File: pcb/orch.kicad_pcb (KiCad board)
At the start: 2 copper layers, 313.6 x 80.8 mm, 139 parts, among them J1 AVR-ISP-6, P1 USB_C_Receptacle_USB2.0, SW1 MX-NoLED, SW10 MX-NoLED, SW11 MX-NoLED, SW12 MX-NoLED, SW13 MX-NoLED, SW14 MX-NoLED, SW15 MX-NoLED, SW16 MX-NoLED, SW17 MX-NoLED, SW18 MX-NoLED, SW19 MX-NoLED, SW2 MX-NoLED, SW20 MX-NoLED, SW21 MX-NoLED, SW22 MX-NoLED, SW23 MX-NoLED, SW24 MX-NoLED, SW25 MX-NoLED, SW26 MX-NoLED, SW27 MX-NoLED, SW28 MX-NoLED, SW29 MX-NoLED, SW3 MX-NoLED, SW30 MX-NoLED, SW31 MX-NoLED, SW32 MX-NoLED, SW33 MX-NoLED, SW34 MX-NoLED, SW35 MX-NoLED, SW36 MX-NoLED, SW37 MX-NoLED, SW38 MX-NoLED, SW39 MX-NoLED, SW4 MX-NoLED, SW40 MX-NoLED, SW41 MX-NoLED, SW42 MX-NoLED, SW43 MX-NoLED, SW44 MX-NoLED, SW45 MX-NoLED, SW46 MX-NoLED, SW47 MX-NoLED, SW48 MX-NoLED, SW49 MX-NoLED, SW5 MX-NoLED, SW50 MX-NoLED, SW51 MX-NoLED, SW52 MX-NoLED, SW53 MX-NoLED, SW54 MX-NoLED, SW55 MX-NoLED, SW56 MX-NoLED, SW57 MX-NoLED, SW58 Reset, SW6 MX-NoLED, SW7 MX-NoLED, SW8 MX-NoLED, SW9 MX-NoLED, U1 ATmega32U4-AU, Y1 16MHz

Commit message: logo
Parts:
- added G***: LOGO, orch:model, B.Cu at (115.6, 177.3)
- added G***: LOGO, orch:logo_small, B.Cu at (240.3, 177.5)
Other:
- board text removed: "orch v0.0.1"

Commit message: new logos
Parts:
- removed the G*** at (115.6, 177.3)
- removed the G*** at (240.3, 177.5)
- added G***: LOGO, orch:htpkbs, B.Cu at (239.8, 177.3)
- added G***: LOGO, orch:orch, B.Cu at (118.4, 177.3)

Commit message: move logos
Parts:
- moved G*** 2.45 mm to (237.4, 176.6)
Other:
- board text added: "htpkbs.com 2021"

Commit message: fix rows and start new traces
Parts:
- moved C4 55.6 mm to (346.4, 154.8), turned to 45 degrees
- moved C3 50.1 mm to (344.0, 144.0), turned to 315 degrees
- moved C5 48.5 mm to (333.2, 159.8), turned to 135 degrees
- moved C6 32.9 mm to (328.2, 146.8), turned to 225 degrees
- moved R5 32.4 mm to (345.2, 117.6)
- moved R4 30.3 mm to (345.2, 114.0)
- moved C7 29.5 mm to (333.0, 141.7), turned to 45 degrees
- moved C8 23.8 mm to (343.4, 130.8), turned to 90 degrees
- moved F1 10.2 mm to (339.3, 115.8), turned to 90 degrees
- moved R6 5.29 mm to (327.9, 154.4), turned to 315 degrees
- moved R2 4.33 mm to (336.3, 130.8)
- moved R1 3.81 mm to (362.7, 138.2)
- moved SW58 3.66 mm to (357.1, 138.2)
- moved J1 3.30 mm to (349.8, 138.2)
- moved R3 2.68 mm to (339.9, 130.8)
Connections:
- U1 pad 36: Net-(U1-Pad36) -> /Row4
- U1 pad 37: Net-(U1-Pad37) -> /Row3
- U1 pad 38: Net-(U1-Pad38) -> /Row2
- U1 pad 39: Net-(U1-Pad39) -> /Row1
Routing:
- net /Col3: track 364.6 -> 0.00 mm, vias 1 -> 0
- net +5V: track 411.1 -> 65.6 mm, vias 12 -> 0
- net /Col1: track 321.2 -> 0.00 mm, vias 1 -> 0
- net /Col5: track 320.2 -> 0.00 mm, vias 1 -> 0
- net /Col2: track 315.5 -> 0.00 mm, vias 1 -> 0
- net /Col6: track 295.5 -> 0.00 mm, vias 1 -> 0
- net /Row3: track 291.3 -> 0.00 mm
- net /Row2: track 287.4 -> 0.00 mm
- net /Row4: track 287.3 -> 0.00 mm
- net /Row1: track 286.7 -> 0.00 mm
- net /Col4: track 279.2 -> 0.00 mm, vias 1 -> 0
- net /Col8: track 239.8 -> 0.00 mm, vias 1 -> 0
- net /Col7: track 196.8 -> 0.00 mm, vias 1 -> 0
- net /Col9: track 170.4 -> 0.00 mm, vias 1 -> 0
- net /Col11: track 157.7 -> 0.00 mm
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
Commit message: v1.0.0
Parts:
- removed the G*** at (118.4, 177.3)
- moved G*** 130.6 mm to (120.1, 119.1)
- turned SW58 to 180 degrees
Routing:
- net +5V: track 65.6 -> 391.6 mm, vias 0 -> 5
- net /Row1: track 0.00 -> 324.0 mm, vias 0 -> 1
- net /Col1: track 0.00 -> 320.8 mm
- net /Row4: track 0.00 -> 320.7 mm, vias 0 -> 3
- net /Row2: track 0.00 -> 308.3 mm, vias 0 -> 1
- net /Col2: track 0.00 -> 302.4 mm
- net /Row3: track 0.00 -> 300.2 mm, vias 0 -> 1
- net /Col3: track 0.00 -> 284.2 mm
- net /Col4: track 0.00 -> 261.7 mm
- net /Col5: track 0.00 -> 238.7 mm
- net /Col6: track 0.00 -> 215.2 mm
- net /Col7: track 0.00 -> 190.0 mm, vias 0 -> 1
- net /Col8: track 0.00 -> 182.8 mm
- net /Col9: track 0.00 -> 165.5 mm
- net /Col10: track 0.00 -> 148.6 mm
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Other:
- board text added: "hack the planet"
- board text added: "orch v1.0.0 2021"
- board text removed: "htpkbs.com 2021"

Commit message: redo power
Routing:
- net +5V: track 391.6 -> 402.4 mm, vias 5 -> 6
- net /Col15: track 89.5 -> 91.9 mm
- net /MOSI: track 18.2 -> 20.3 mm
- net /D+: track 15.5 -> 16.8 mm
- net /Reset: track 38.4 -> 39.7 mm
- net /D-: track 14.9 -> 15.7 mm
- net /Col14: track 93.7 -> 93.2 mm, vias 3 -> 4
- net GND: vias 3 -> 7

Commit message: v2!
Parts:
- added D25: 1N4148, orch:D_DO-35_SOD27_P5.08mm_Horizontal, B.Cu at (165.7, 172.6)
- added D29: 1N4148, orch:D_DO-35_SOD27_P5.08mm_Horizontal, B.Cu at (201.1, 172.6)
- added D55: 1N4148, orch:D_DO-35_SOD27_P5.08mm_Horizontal, B.Cu at (348.1, 155.8)
- added D66: SK6812, LED_SMD:LED_SK6812_PLCC4_5.0x5.0mm_P3.2mm, B.Cu at (306.9, 163.8)
- added SW25: MX-NoLED, orch:MX-2U-NoLED, F.Cu at (183.4, 168.6)
- added SW29: MX-NoLED, orch:MX-1U-NoLED, F.Cu at (192.9, 168.6)
- added SW55: Rotary_Encoder_Switch, orch:RotaryEncoder_Alps_EC11E-Switch_Vertical_H20mm, F.Cu at (330.5, 149.4)
- SW24: footprint orch:MX-2U-NoLED -> orch:MX-1U-NoLED
- SW51: renamed from SW49; footprint orch:MX-2.25U-NoLED -> orch:MX-1.75U-NoLED
- moved D63 102.0 mm to (107.4, 121.1)
- moved D65 99.5 mm to (202.4, 159.2)
- moved D62 77.4 mm to (202.4, 121.1)
- moved G*** 71.9 mm to (77.4, 176.9)
- moved D64 45.0 mm to (107.4, 159.1)
- moved R1 26.3 mm to (349.4, 115.5), turned to 90 degrees
- moved D61 23.4 mm to (306.9, 121.2)
- moved C1 23.1 mm to (350.9, 138.7), turned to 45 degrees
- moved C2 23.1 mm to (347.4, 142.2)
- moved Y1 23.1 mm to (345.7, 137.0)
- moved R6 23.0 mm to (326.3, 131.5)
- moved C4 22.6 mm to (345.2, 132.2)
- moved C6 22.4 mm to (327.3, 124.5)
- moved U1 22.4 mm to (336.5, 128.3)
- moved C7 22.1 mm to (332.0, 119.6)
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- renumbered D25 to D26, D26 to D27, D27 to D28, D28 to D30, D29 to D31, D30 to D32, D31 to D33, D32 to D34, D33 to D35, D34 to D36, D35 to D37, D36 to D38, D37 to D39, D38 to D40, D39 to D41, D40 to D42, D41 to D43, D42 to D44, D43 to D45, D44 to D46, D45 to D47, D46 to D48, D47 to D49, D48 to D50, D49 to D51, D50 to D52, D51 to D53, D52 to D54, D53 to D56, D54 to D57, D55 to D58, D56 to D59, D57 to D60, D58 to D61, D59 to D62, D60 to D63, D61 to D64, D62 to D65, SW25 to SW26, SW26 to SW27, SW27 to SW28, SW28 to SW30, SW29 to SW31, SW30 to SW32, SW31 to SW33, SW32 to SW34, SW33 to SW35, SW34 to SW36, SW35 to SW37, SW36 to SW38, SW37 to SW39, SW38 to SW40, SW39 to SW41, SW40 to SW42, SW41 to SW43, SW42 to SW44, SW43 to SW45, SW44 to SW46, SW45 to SW47, SW46 to SW48, SW47 to SW49, SW48 to SW50, SW50 to SW52, SW51 to SW53, SW52 to SW54, SW53 to SW56, SW54 to SW57, SW55 to SW58, SW56 to SW59, SW57 to SW60, SW58 to SW61
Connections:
- U1 pad 1: Net-(U1-Pad1) -> /Col14
- U1 pad 12: /Col14 -> /Row2
- U1 pad 18: /Col13 -> /Row3
- U1 pad 19: /Col12 -> /Row4
- U1 pad 20: /Col11 -> /Col13
- U1 pad 21: /Col10 -> /Col12
- U1 pad 22: /Col9 -> /Col11
- U1 pad 25: /Col8 -> /Col10
- U1 pad 26: /Col7 -> /Col9
- U1 pad 27: /Col6 -> /Col8
- U1 pad 28: /Col5 -> /Col7
- U1 pad 29: /Col4 -> /Col6
- U1 pad 30: /Col3 -> /Col5
- U1 pad 31: /Col2 -> /Col4
- U1 pad 32: /Col1 -> /Col3
- U1 pad 36: /Row4 -> /Col1
- U1 pad 37: /Row3 -> /Col2
- U1 pad 38: /Row2 -> /RGB
- U1 pad 39: /Row1 -> /RotaryA
- U1 pad 40: /RGB -> /RotaryB
- U1 pad 41: /Col15 -> /Row1
- U1 pad 8: Net-(U1-Pad8) -> /Col15
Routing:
- net +5V: track 402.4 -> 590.0 mm, vias 6 -> 9
- net Net-(D65-Pad4): track 0.00 -> 112.8 mm
- net Net-(D64-Pad4): track 39.8 -> 102.3 mm
- net Net-(D61-Pad4): track 41.2 -> 100.9 mm
- net /Row4: track 320.7 -> 361.4 mm, vias 3 -> 0
- net /Row3: track 300.6 -> 337.3 mm, vias 1 -> 2
- net /RotaryB: track 0.00 -> 36.3 mm, vias 0 -> 2
- net /RotaryA: track 0.00 -> 30.2 mm, vias 0 -> 2
- net GND: track 86.7 -> 112.9 mm, vias 7 -> 37
- net Net-(D62-Pad4): track 66.6 -> 91.4 mm
- net Net-(D25-Pad2): track 0.00 -> 23.4 mm
- net Net-(P1-PadA7): track 27.0 -> 8.40 mm, vias 1 -> 0
- net /Col14: track 93.2 -> 111.0 mm, vias 4 -> 0
- net Net-(P1-PadA6): track 25.2 -> 8.35 mm, vias 1 -> 0
- net /Reset: track 39.7 -> 56.0 mm, vias 2 -> 0
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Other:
- board text added: "RESET"
- board text added: "orch v2"
- board text removed: "orch v1.0.0 2021"

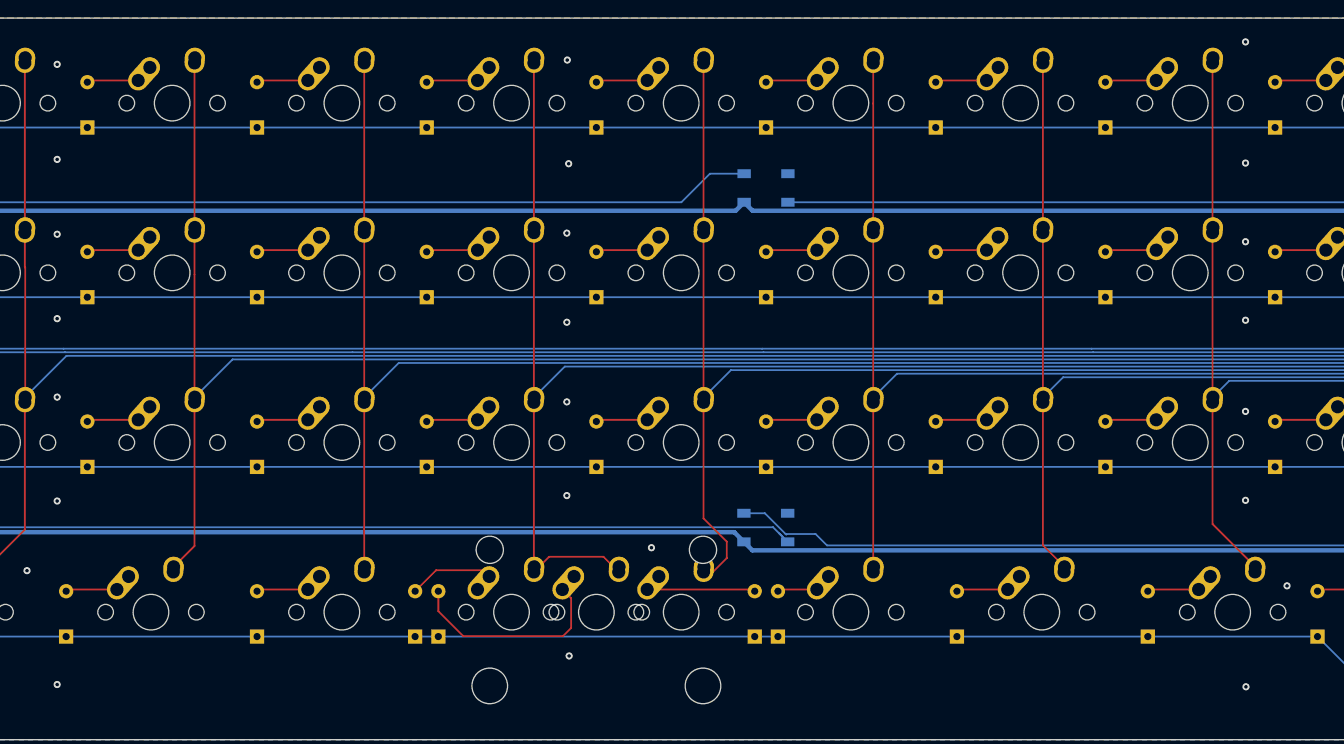
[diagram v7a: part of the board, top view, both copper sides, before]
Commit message: add isp label
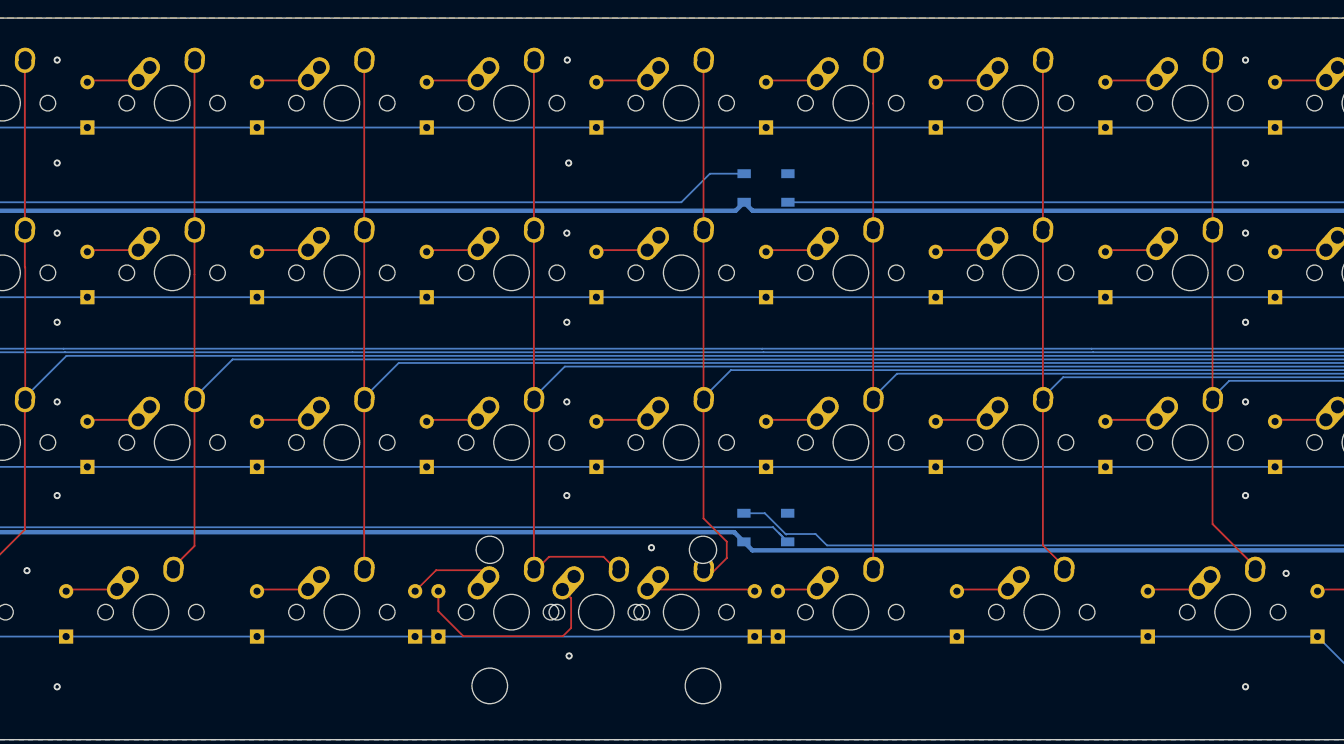
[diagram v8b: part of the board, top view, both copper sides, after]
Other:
- board text added: "ISP"
